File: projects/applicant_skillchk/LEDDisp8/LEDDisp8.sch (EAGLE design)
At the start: 26 parts, among them J1 4X2, J2 3X1A

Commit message: 回路図作成
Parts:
- added H1, H2, H3, H4: HOLE3.3M3BOLT, Hole:HOLE3.3M3BOLT
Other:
- moved on the sheet: J11-1, J11-2, J11-3, J11-4, J12-1, J12-2, J12-3, J12-4, J2-1, J2-2, J2-3
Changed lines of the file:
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@@
 <part name="GND9" library="supply1" deviceset="GND" device=""/>
 <part name="P+9" library="supply1" deviceset="+5V" device=""/>
+<part name="H1" library="Hole" deviceset="HOLE3.3" device="M3BOLT"/>
+<part name="H2" library="Hole" deviceset="HOLE3.3" device="M3BOLT"/>
+<part name="H3" library="Hole" deviceset="HOLE3.3" device="M3BOLT"/>
+<part name="H4" library="Hole" deviceset="HOLE3.3" device="M3BOLT"/>
 </parts>
 <sheets>
 <sheet>
 <plain>
-<wire x1="-40.64" y1="104.14" x2="-40.64" y2="45.72" width="0.1524" layer="97"/>
-<wire x1="-40.64" y1="45.72" x2="-40.64" y2="-22.86" width="0.1524" layer="97"/>
+<wire x1="-40.64" y1="104.14" x2="-40.64" y2="63.5" width="0.1524" layer="97"/>
+<wire x1="-40.64" y1="63.5" x2="-40.64" y2="20.32" width="0.1524" layer="97"/>
+<wire x1="-40.64" y1="20.32" x2="-40.64" y2="-22.86" width="0.1524" layer="97"/>
 <wire x1="-40.64" y1="-22.86" x2="-10.16" y2="-22.86" width="0.1524" layer="97"/>
 <wire x1="-10.16" y1="-22.86" x2="137.16" y2="-22.86" width="0.1524" layer="97"/>
@@
 <wire x1="137.16" y1="104.14" x2="-10.16" y2="104.14" width="0.1524" layer="97"/>
 <wire x1="-10.16" y1="104.14" x2="-40.64" y2="104.14" width="0.1524" layer="97"/>
-<wire x1="-40.64" y1="45.72" x2="-10.16" y2="45.72" width="0.1524" layer="97"/>
-<wire x1="-10.16" y1="45.72" x2="-10.16" y2="43.18" width="0.1524" layer="97"/>
-<wire x1="-10.16" y1="43.18" x2="-10.16" y2="-22.86" width="0.1524" layer="97"/>
-<wire x1="-10.16" y1="43.18" x2="-10.16" y2="104.14" width="0.1524" layer="97"/>
+<wire x1="-40.64" y1="63.5" x2="-10.16" y2="63.5" width="0.1524" layer="97"/>
+<wire x1="-10.16" y1="63.5" x2="-10.16" y2="43.18" width="0.1524" layer="97"/>
+<wire x1="-10.16" y1="43.18" x2="-10.16" y2="20.32" width="0.1524" layer="97"/>
+<wire x1="-10.16" y1="20.32" x2="-10.16" y2="-22.86" width="0.1524" layer="97"/>
+<wire x1="-10.16" y1="43.18" x2="-10.16" y2="63.5" width="0.1524" layer="97"/>
+<wire x1="-10.16" y1="63.5" x2="-10.16" y2="104.14" width="0.1524" layer="97"/>
+<wire x1="-40.64" y1="20.32" x2="-10.16" y2="20.32" width="0.1524" layer="97"/>
 </plain>
 <instances>
-<instance part="J1" gate="1-1" x="-27.94" y="30.48"/>
-<instance part="J1" gate="1-3" x="-27.94" y="20.32"/>
-<instance part="J1" gate="1-2" x="-27.94" y="25.4"/>
-<instance part="J1" gate="1-4" x="-27.94" y="15.24"/>
-<instance part="J1" gate="2-1" x="-27.94" y="10.16"/>
-<instance part="J1" gate="2-2" x="-27.94" y="5.08"/>
-<instance part="J1" gate="2-3" x="-27.94" y="0"/>
-<instance part="J1" gate="2-4" x="-27.94" y="-5.08"/>
-<instance part="J2" gate="-1" x="-20.32" y="78.74" rot="R270"/>
-<instance part="J2" gate="-2" x="-25.4" y="78.74" rot="R270"/>
-<instance part="J2" gate="-3" x="-30.48" y="78.74" rot="R270"/>
+<instance part="J1" gate="1-1" x="-27.94" y="58.42"/>
+<instance part="J1" gate="1-3" x="-27.94" y="48.26"/>
+<instance part="J1" gate="1-2" x="-27.94" y="53.34"/>
+<instance part="J1" gate="1-4" x="-27.94" y="43.18"/>
+<instance part="J1" gate="2-1" x="-27.94" y="38.1"/>
+<instance part="J1" gate="2-2" x="-27.94" y="33.02"/>
+<instance part="J1" gate="2-3" x="-27.94" y="27.94"/>
+<instance part="J1" gate="2-4" x="-27.94" y="22.86"/>
+<instance part="J2" gate="-1" x="-20.32" y="91.44" rot="R270"/>
+<instance part="J2" gate="-2" x="-25.4" y="91.44" rot="R270"/>
+<instance part="J2" gate="-3" x="-30.48" y="91.44" rot="R270"/>
 <instance part="R1" gate="G$1" x="43.18" y="76.2" rot="R90"/>
 <instance part="LED1" gate="G$1" x="43.18" y="88.9"/>
 <instance part="TR1" gate="G$1" x="40.64" y="58.42"/>
-<instance part="P+1" gate="1" x="-25.4" y="58.42"/>
-<instance part="GND1" gate="1" x="-20.32" y="58.42"/>
+<instance part="P+1" gate="1" x="-25.4" y="71.12"/>
+<instance part="GND1" gate="1" x="-20.32" y="71.12"/>
 <instance part="GND7" gate="1" x="53.34" y="48.26" rot="R90"/>
 <instance part="P+2" gate="1" x="33.02" y="96.52" rot="R270"/>
@@
 <instance part="GND9" gate="1" x="129.54" y="-17.78" rot="R90"/>
 <instance part="P+9" gate="1" x="109.22" y="30.48" rot="R270"/>
+<instance part="H1" gate="G$1" x="-25.4" y="5.08"/>
+<instance part="H2" gate="G$1" x="-25.4" y="0"/>
+<instance part="H3" gate="G$1" x="-25.4" y="-5.08"/>
+<instance part="H4" gate="G$1" x="-25.4" y="-10.16"/>
 </instances>
 <busses>
@@
 <segment>
 <pinref part="J2" gate="-2" pin="S"/>
-<wire x1="-25.4" y1="83.82" x2="-25.4" y2="58.42" width="0.1524" layer="91"/>
+<wire x1="-25.4" y1="96.52" x2="-25.4" y2="71.12" width="0.1524" layer="91"/>
 </segment>
 </net>
 <net name="GND" class="0">
 <segment>
-<wire x1="-30.48" y1="81.28" x2="-30.48" y2="83.82" width="0.1524" layer="91"/>
-<wire x1="-30.48" y1="83.82" x2="-30.48" y2="88.9" width="0.1524" layer="91"/>
-<wire x1="-30.48" y1="88.9" x2="-20.32" y2="88.9" width="0.1524" layer="91"/>
-<wire x1="-20.32" y1="88.9" x2="-20.32" y2="83.82" width="0.1524" layer="91"/>
+<wire x1="-30.48" y1="93.98" x2="-30.48" y2="96.52" width="0.1524" layer="91"/>
+<wire x1="-30.48" y1="96.52" x2="-30.48" y2="101.6" width="0.1524" layer="91"/>
+<wire x1="-30.48" y1="101.6" x2="-20.32" y2="101.6" width="0.1524" layer="91"/>
+<wire x1="-20.32" y1="101.6" x2="-20.32" y2="96.52" width="0.1524" layer="91"/>
 <pinref part="GND1" gate="1" pin="GND"/>
-<wire x1="-20.32" y1="83.82" x2="-20.32" y2="81.28" width="0.1524" layer="91"/>
-<wire x1="-20.32" y1="60.96" x2="-20.32" y2="83.82" width="0.1524" layer="91"/>
-<junction x="-20.32" y="83.82"/>
+<wire x1="-20.32" y1="96.52" x2="-20.32" y2="93.98" width="0.1524" layer="91"/>
+<wire x1="-20.32" y1="73.66" x2="-20.32" y2="96.52" width="0.1524" layer="91"/>
+<junction x="-20.32" y="96.52"/>
 <pinref part="J2" gate="-1" pin="S"/>
 <pinref part="J2" gate="-3" pin="S"/>
-<junction x="-30.48" y="83.82"/>
+<junction x="-30.48" y="96.52"/>
 </segment>
 <segment>
@@
 <segment>
 <pinref part="J1" gate="1-1" pin="S"/>
-<wire x1="-33.02" y1="30.48" x2="-22.86" y2="30.48" width="0.1524" layer="91"/>
-<label x="-22.86" y="30.48" size="1.778" layer="95" xref="yes"/>
+<wire x1="-33.02" y1="58.42" x2="-22.86" y2="58.42" width="0.1524" layer="91"/>
+<label x="-22.86" y="58.42" size="1.778" layer="95" xref="yes"/>
 </segment>
 <segment>
@@
 <segment>
 <pinref part="J1" gate="1-2" pin="S"/>
-<wire x1="-33.02" y1="25.4" x2="-22.86" y2="25.4" width="0.1524" layer="91"/>
-<label x="-22.86" y="25.4" size="1.778" layer="95" xref="yes"/>
+<wire x1="-33.02" y1="53.34" x2="-22.86" y2="53.34" width="0.1524" layer="91"/>
+<label x="-22.86" y="53.34" size="1.778" layer="95" xref="yes"/>
 </segment>
 <segment>
@@
 <segment>
 <pinref part="J1" gate="1-3" pin="S"/>
-<wire x1="-33.02" y1="20.32" x2="-22.86" y2="20.32" width="0.1524" layer="91"/>
-<label x="-22.86" y="20.32" size="1.778" layer="95" xref="yes"/>
+<wire x1="-33.02" y1="48.26" x2="-22.86" y2="48.26" width="0.1524" layer="91"/>
+<label x="-22.86" y="48.26" size="1.778" layer="95" xref="yes"/>
 </segment>
 <segment>
@@
 <segment>
 <pinref part="J1" gate="1-4" pin="S"/>
-<wire x1="-33.02" y1="15.24" x2="-22.86" y2="15.24" width="0.1524" layer="91"/>
-<label x="-22.86" y="15.24" size="1.778" layer="95" xref="yes"/>
+<wire x1="-33.02" y1="43.18" x2="-22.86" y2="43.18" width="0.1524" layer="91"/>
+<label x="-22.86" y="43.18" size="1.778" layer="95" xref="yes"/>
 </segment>
 <segment>
@@
 <segment>
 <pinref part="J1" gate="2-1" pin="S"/>
-<wire x1="-33.02" y1="10.16" x2="-22.86" y2="10.16" width="0.1524" layer="91"/>
-<label x="-22.86" y="10.16" size="1.778" layer="95" xref="yes"/>
+<wire x1="-33.02" y1="38.1" x2="-22.86" y2="38.1" width="0.1524" layer="91"/>
+<label x="-22.86" y="38.1" size="1.778" layer="95" xref="yes"/>
 </segment>
 <segment>
@@
 <segment>
 <pinref part="J1" gate="2-2" pin="S"/>
-<wire x1="-33.02" y1="5.08" x2="-22.86" y2="5.08" width="0.1524" layer="91"/>
-<label x="-22.86" y="5.08" size="1.778" layer="95" xref="yes"/>
+<wire x1="-33.02" y1="33.02" x2="-22.86" y2="33.02" width="0.1524" layer="91"/>
+<label x="-22.86" y="33.02" size="1.778" layer="95" xref="yes"/>
 </segment>
 <segment>
@@
 <segment>
 <pinref part="J1" gate="2-3" pin="S"/>
-<wire x1="-33.02" y1="0" x2="-22.86" y2="0" width="0.1524" layer="91"/>
-<label x="-22.86" y="0" size="1.778" layer="95" xref="yes"/>
+<wire x1="-33.02" y1="27.94" x2="-22.86" y2="27.94" width="0.1524" layer="91"/>
+<label x="-22.86" y="27.94" size="1.778" layer="95" xref="yes"/>
 </segment>
 <segment>
@@
 <segment>
 <pinref part="J1" gate="2-4" pin="S"/>
-<wire x1="-33.02" y1="-5.08" x2="-22.86" y2="-5.08" width="0.1524" layer="91"/>
-<label x="-22.86" y="-5.08" size="1.778" layer="95" xref="yes"/>
-</segment>
-<segment>
+<wire x1="-33.02" y1="22.86" x2="-22.86" y2="22.86" width="0.1524" layer="91"/>
+<label x="-22.86" y="22.86" size="1.778" layer="95" xref="yes"/>
+</segment>
+<segment>

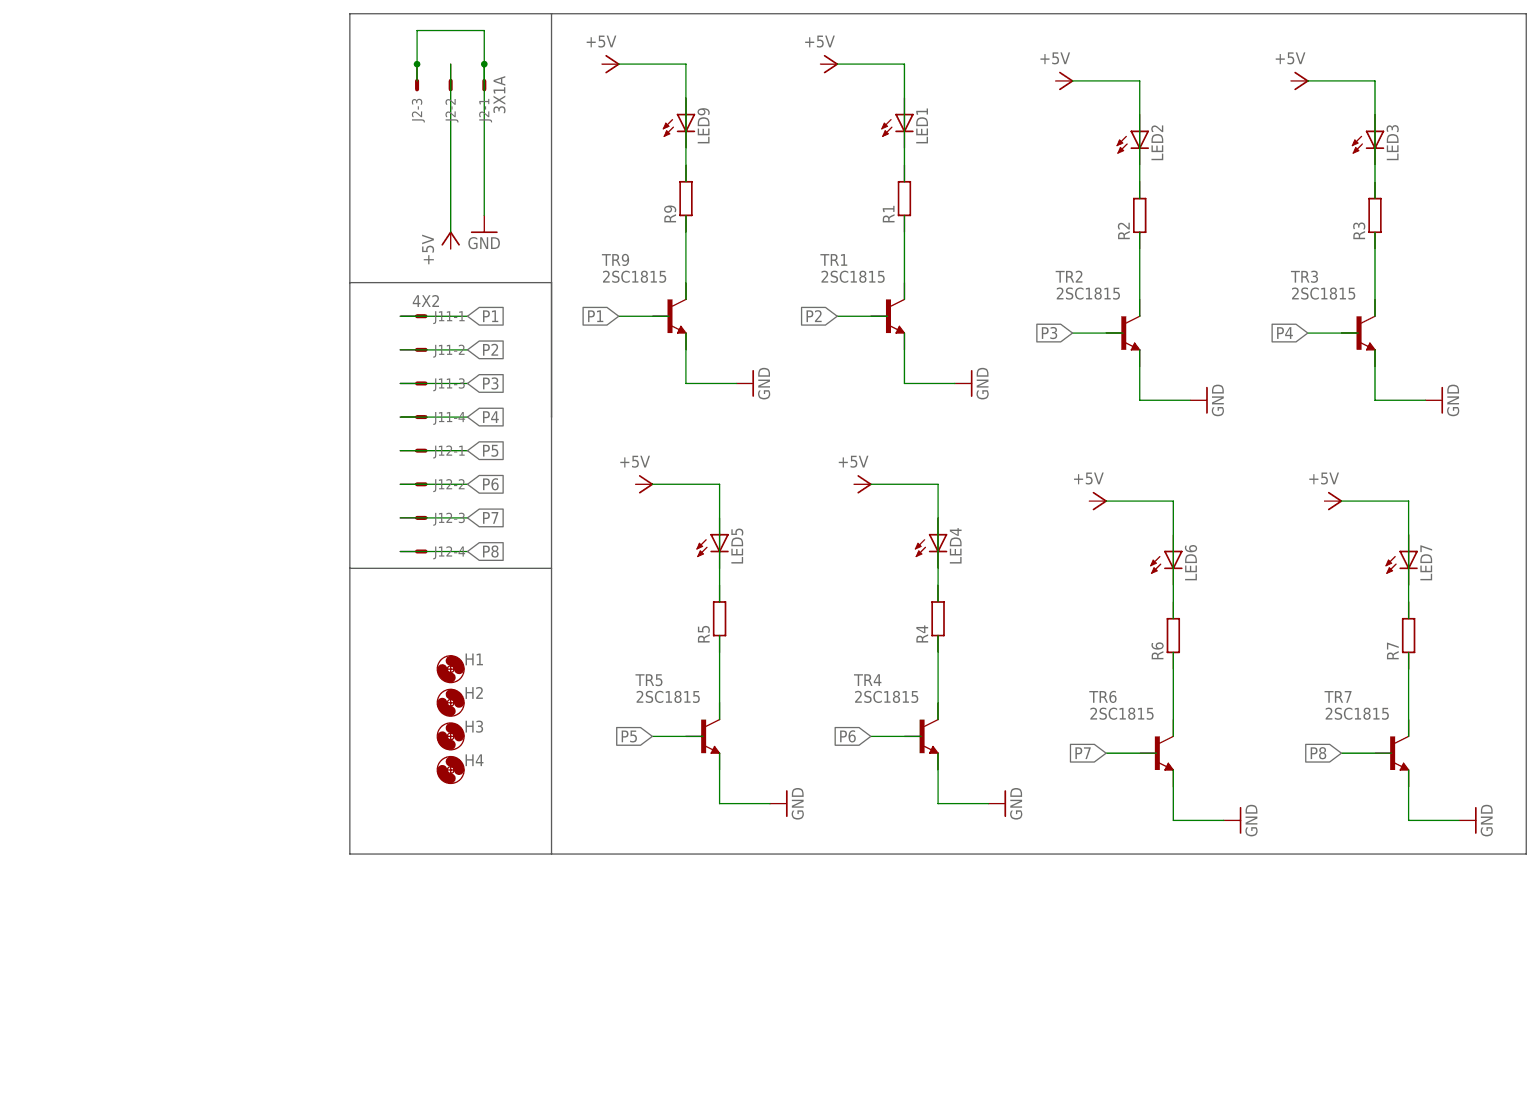
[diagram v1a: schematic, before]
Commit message: 回路図の修正
schemeticファイルの余計な配線を削除
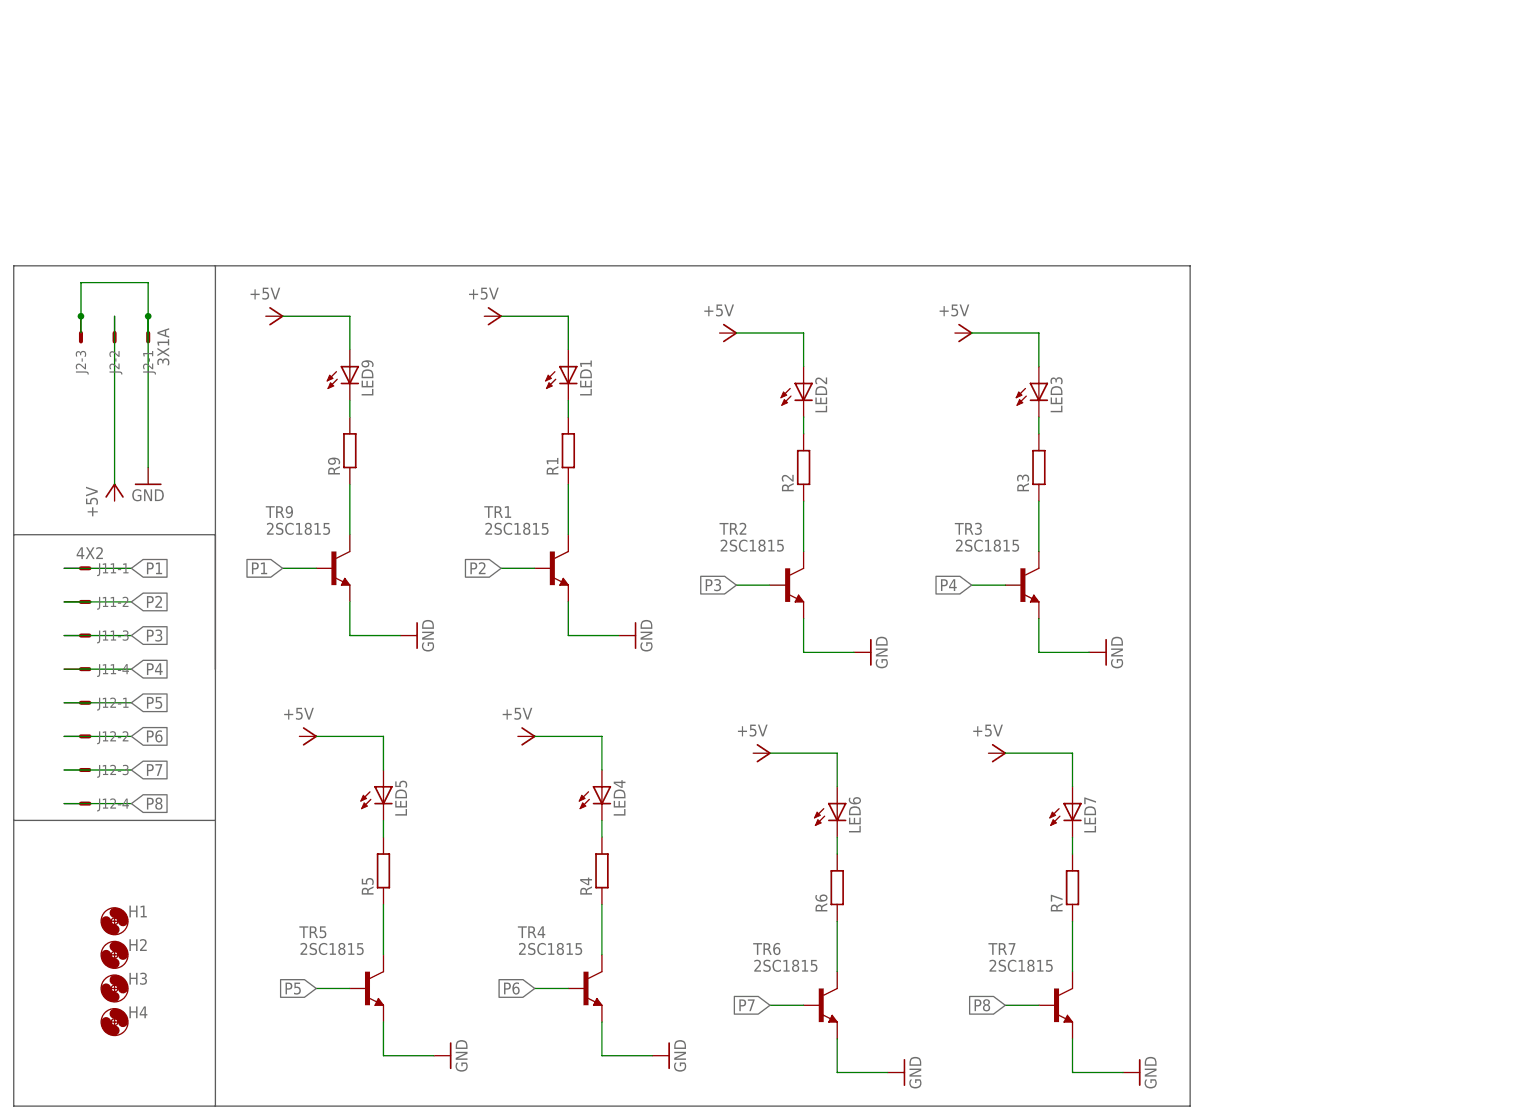
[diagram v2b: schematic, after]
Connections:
- new net N$1: R1.1, TR1.C
- new net N$10: LED3.A
- new net N$11: R4.1, TR4.C
- new net N$12: LED4.A
- new net N$13: R5.1, TR5.C
- new net N$14: LED5.A
- new net N$15: R6.1, TR6.C
- new net N$16: LED6.A
- new net N$17: R7.1, TR7.C
- new net N$18: LED7.A
- new net N$19: LED1.C, R1.2
- new net N$21: LED2.C, R2.2
- new net N$22: LED6.C, R6.2
- new net N$23: LED3.C, R3.2
- new net N$24: LED4.C, R4.2
- new net N$25: LED7.C, R7.2
- new net N$26: LED5.C, R5.2
- new net N$3: LED1.A
- new net N$4: R9.1, TR9.C
- new net N$5: LED9.C, R9.2
- new net N$6: LED9.A
- new net N$7: R2.1, TR2.C
- new net N$8: LED2.A
- new net N$9: R3.1, TR3.C
- net GND: now also TR1.E, TR2.E, TR3.E, TR4.E, TR5.E, TR6.E, TR7.E, TR9.E
- net P1: now also TR9.B
- net P2: now also TR1.B
- net P3: now also TR2.B
- net P4: now also TR3.B
- net P5: now also TR5.B
- net P6: now also TR4.B
- net P7: now also TR6.B
- net P8: now also TR7.B
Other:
- moved on the sheet: H1, H2, H3, H4, J11-1, J11-2, J11-3, J11-4, J12-1, J12-2, J12-3, J12-4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
